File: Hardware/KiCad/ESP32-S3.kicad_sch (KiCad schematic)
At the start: 34 parts, among them J1 UJ20-C-H-G-SMT-1-P16-TR, J4 RJ45, U1 ESP32-S3-WROOM-1, U5 WE-TVS-82400102, U7 AP7333-33SRG-7

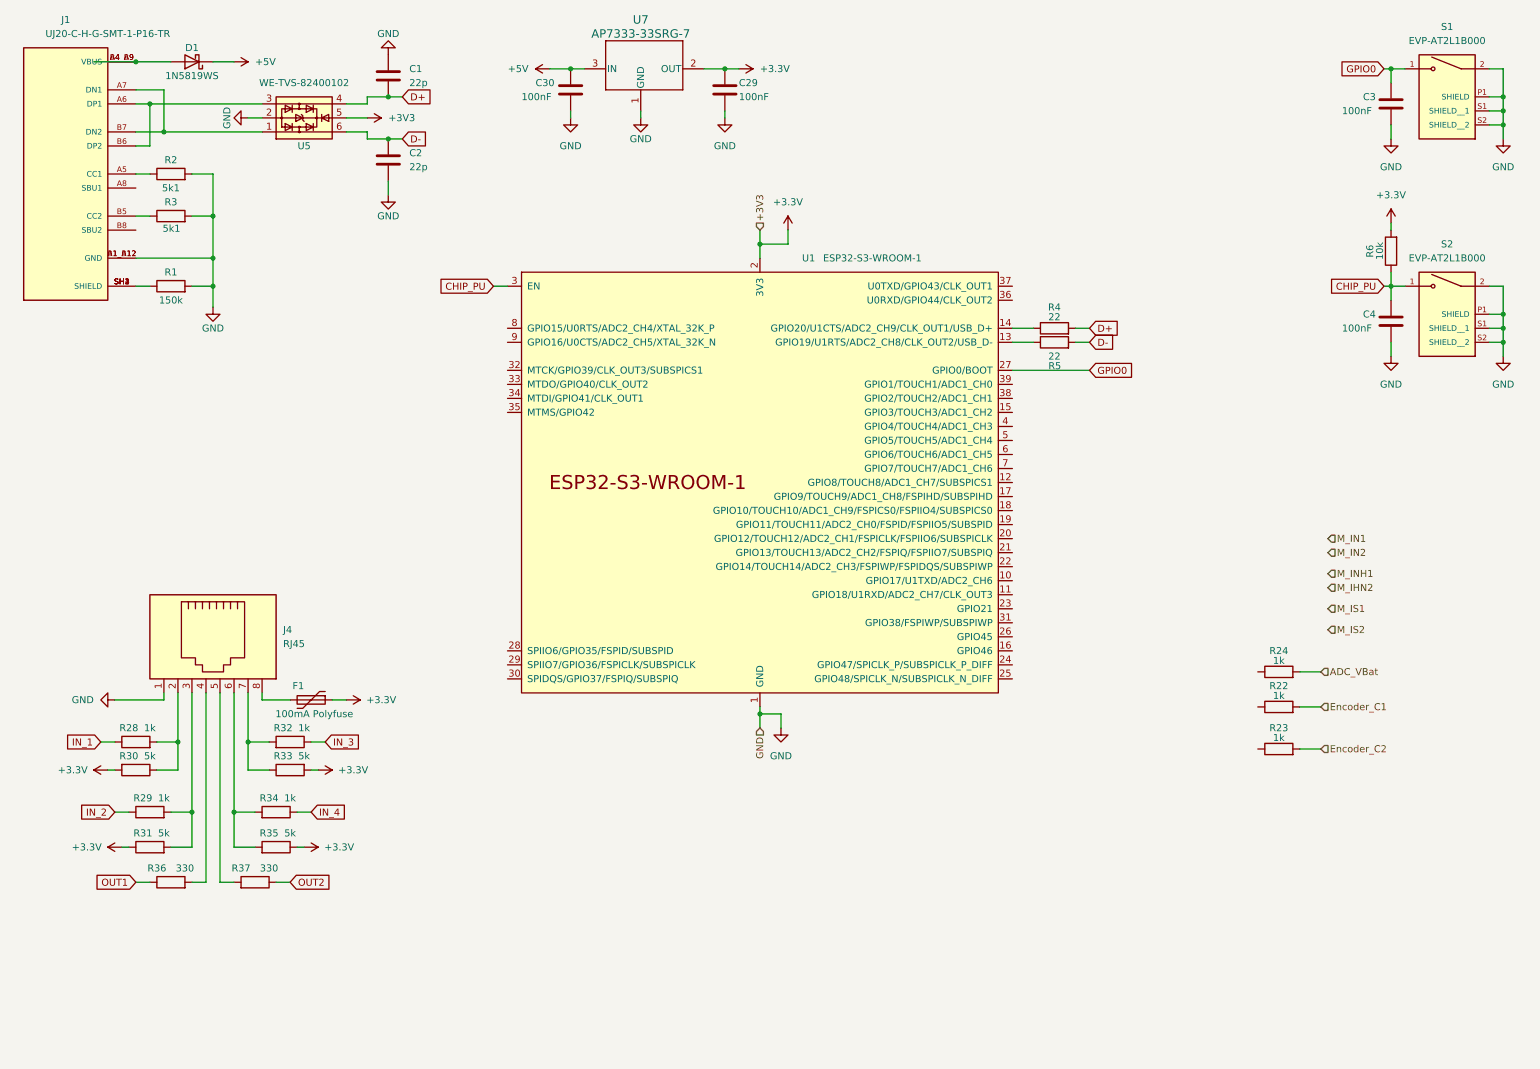
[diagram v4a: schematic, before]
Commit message: add ESD protection to inputs
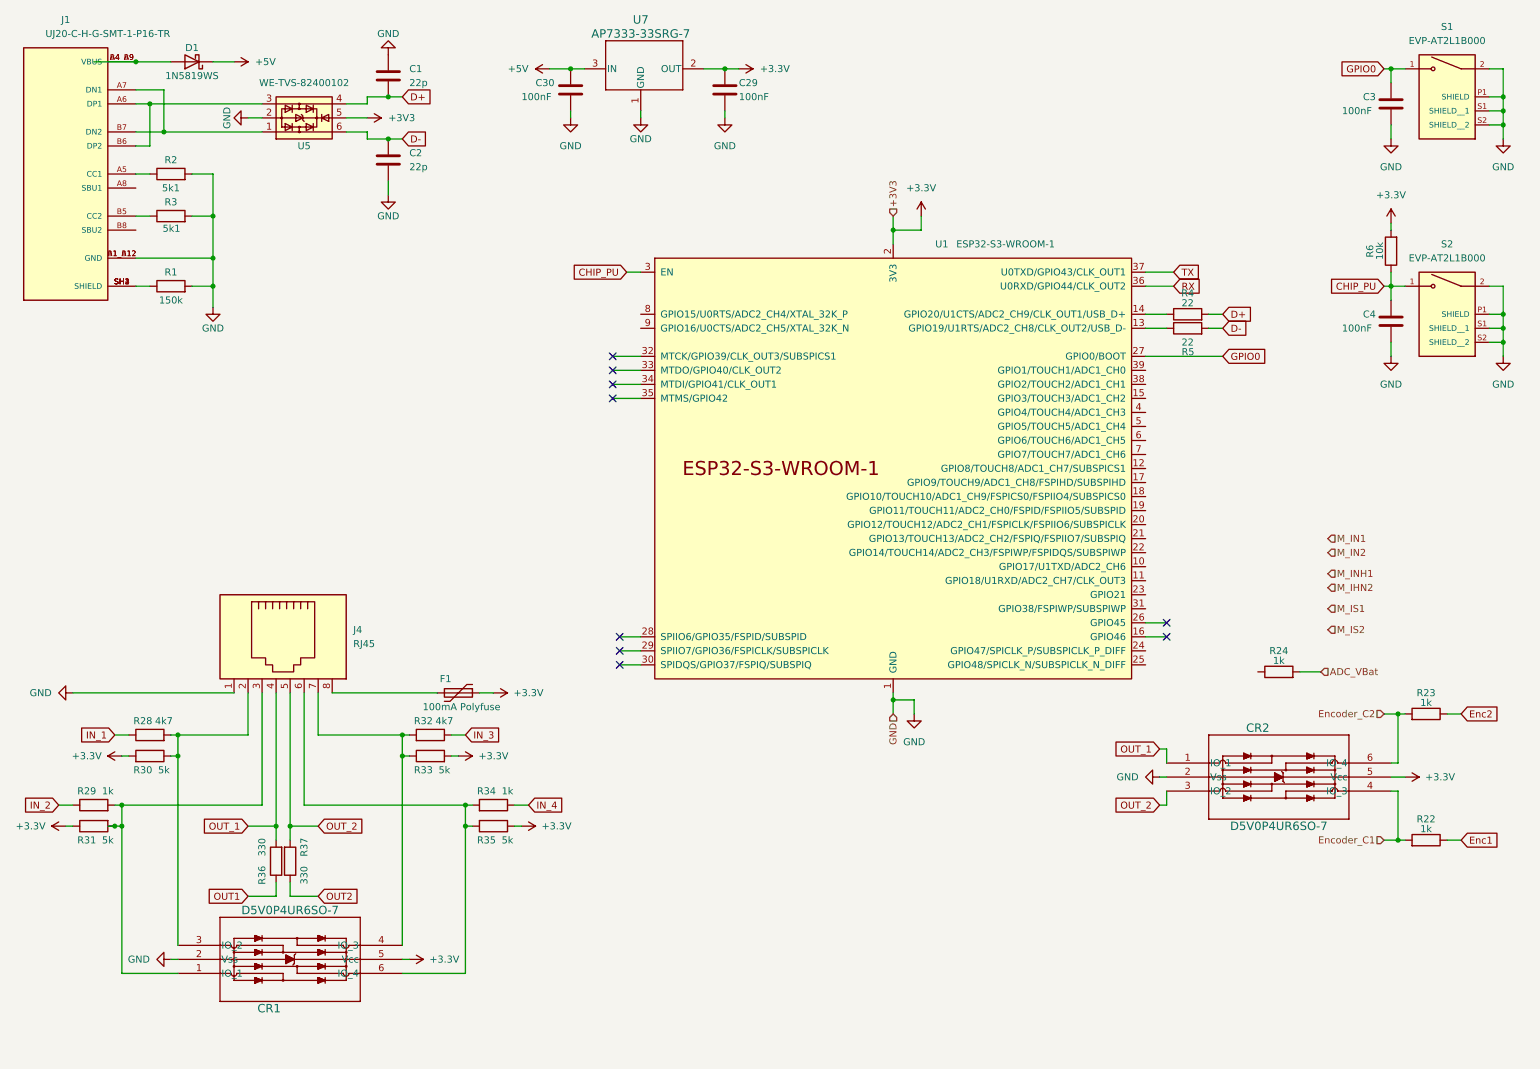
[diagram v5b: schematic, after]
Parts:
- added CR1, CR2: D5V0P4UR6SO-7, BugWiper_lib:SOT26_DIO, symbol BugWiper_Lib:D5V0P4UR6SO-7
- R28, R32: value 1k -> 4k7
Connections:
- net +3.3V: now also CR1.5 (Vcc), CR2.5 (Vcc)
- net Encoder_C1: now also CR2.4 (IO_3)
- net Encoder_C2: now also CR2.6 (IO_4)
- net GND: now also CR1.2 (Vss), CR2.2 (Vss)
- net at J4.7, R32.2, R33.1: now also CR1.4 (IO_3)
- net at J4.2, R28.2, R30.1: now also CR1.3 (IO_2)
- net at J4.3, R29.2, R31.2: now also CR1.1 (IO_1)
- net OUT_1: now reaches J4.4, R36.2
- net OUT_1: now also CR2.1 (IO_1)
- net OUT_2: now reaches J4.5, R37.2
- net OUT_2: now also CR2.3 (IO_2)
- net at J4.6, R34.2, R35.2: now also CR1.6 (IO_4)
- net RX: now reaches U1.36 (U0RXD/GPIO44/CLK_OUT2)
- net TX: now reaches U1.37 (U0TXD/GPIO43/CLK_OUT1)
- net Enc1: now reaches R22.1
- net Enc2: now reaches R23.1
- no-connect marks 0 -> 9
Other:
- moved on the sheet: F1, J4, R22, R23, R28, R29, R30, R31, R32, R33, R34, R35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

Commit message: add debug connector, arrange foodprints and add NTC and connect to GPIOs to ESP32
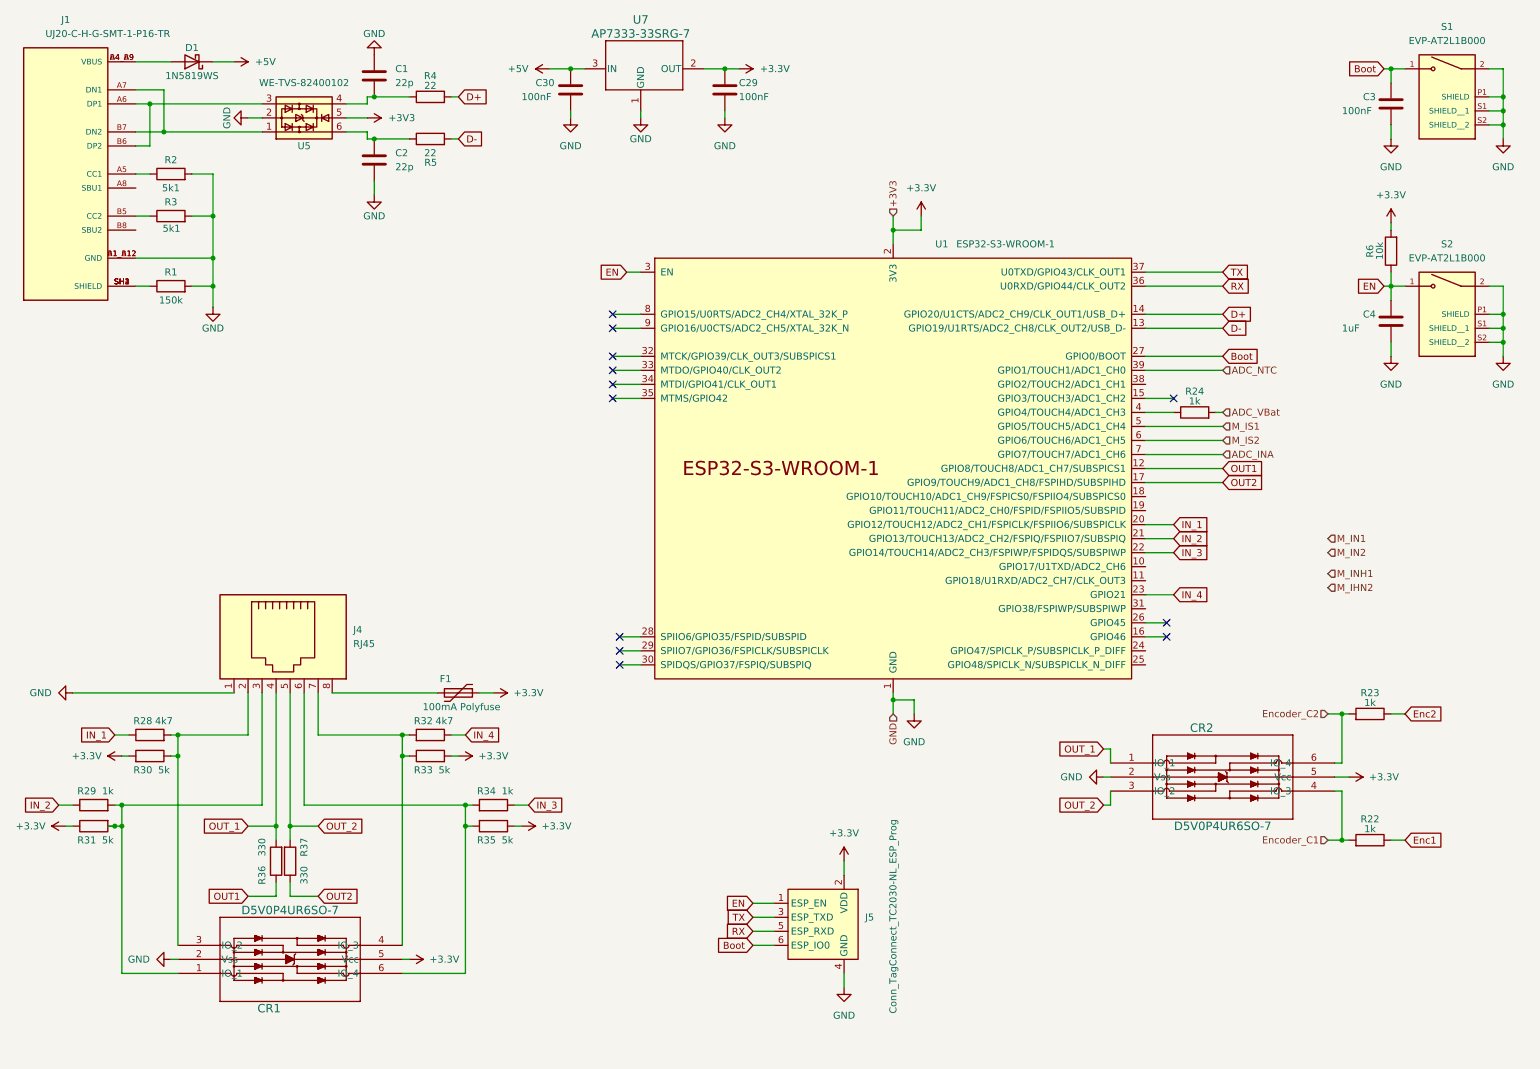
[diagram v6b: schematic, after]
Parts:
- added J5: Conn_TagConnect_TC2030-NL_ESP_Prog, Connector:Tag-Connect_TC2030-IDC-NL_2x03_P1.27mm_Vertical, symbol BugWiper_Lib:Conn_TagConnect_TC2030-NL_ESP_Prog
- C4: value 100nF -> 1uF
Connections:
- net +3.3V: now also J5.2 (VDD)
- net D+: now also U1.14 (GPIO20/U1CTS/ADC2_CH9/CLK_OUT1/USB_D+); no longer C1.2, U5.4
- net D-: now also U1.13 (GPIO19/U1RTS/ADC2_CH8/CLK_OUT2/USB_D-); no longer C2.1, U5.6
- net GND: now also J5.4 (GND)
- net IN_1: now also U1.20 (GPIO12/TOUCH12/ADC2_CH1/FSPICLK/FSPIIO6/SUBSPICLK)
- net IN_2: now also U1.21 (GPIO13/TOUCH13/ADC2_CH2/FSPIQ/FSPIIO7/SUBSPIQ)
- net IN_3: now also R34.1, U1.22 (GPIO14/TOUCH14/ADC2_CH3/FSPIWP/FSPIDQS/SUBSPIWP); no longer R32.1
- net IN_4: now also R32.1, U1.23 (GPIO21); no longer R34.1
- net M_IS1: now also U1.5 (GPIO5/TOUCH5/ADC1_CH4)
- net M_IS2: now also U1.6 (GPIO6/TOUCH6/ADC1_CH5)
- net OUT1: now also U1.12 (GPIO8/TOUCH8/ADC1_CH7/SUBSPICS1)
- net OUT2: now also U1.17 (GPIO9/TOUCH9/ADC1_CH8/FSPIHD/SUBSPIHD)
- net RX: now also J5.5 (ESP_RXD)
- net TX: now also J5.3 (ESP_TXD)
- net at R4.1: now also C1.2, U5.4; no longer U1.14 (GPIO20/U1CTS/ADC2_CH9/CLK_OUT1/USB_D+)
- net at R5.1: now also C2.1, U5.6; no longer U1.13 (GPIO19/U1RTS/ADC2_CH8/CLK_OUT2/USB_D-)
- net ADC_NTC: now reaches U1.39 (GPIO1/TOUCH1/ADC1_CH0)
- net at U1.4 (GPIO4/TOUCH4/ADC1_CH3): now also R24.1
- net ADC_INA: now reaches U1.7 (GPIO7/TOUCH7/ADC1_CH6)
- net CHIP_PU renamed EN
- net EN: now also J5.1 (ESP_EN)
- net GPIO0 renamed Boot
- net Boot: now also J5.6 (ESP_IO0)
- no-connect marks 9 -> 12
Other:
- moved on the sheet: C1, C2, CR2, R22, R23, R24

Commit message: add resistor arrays
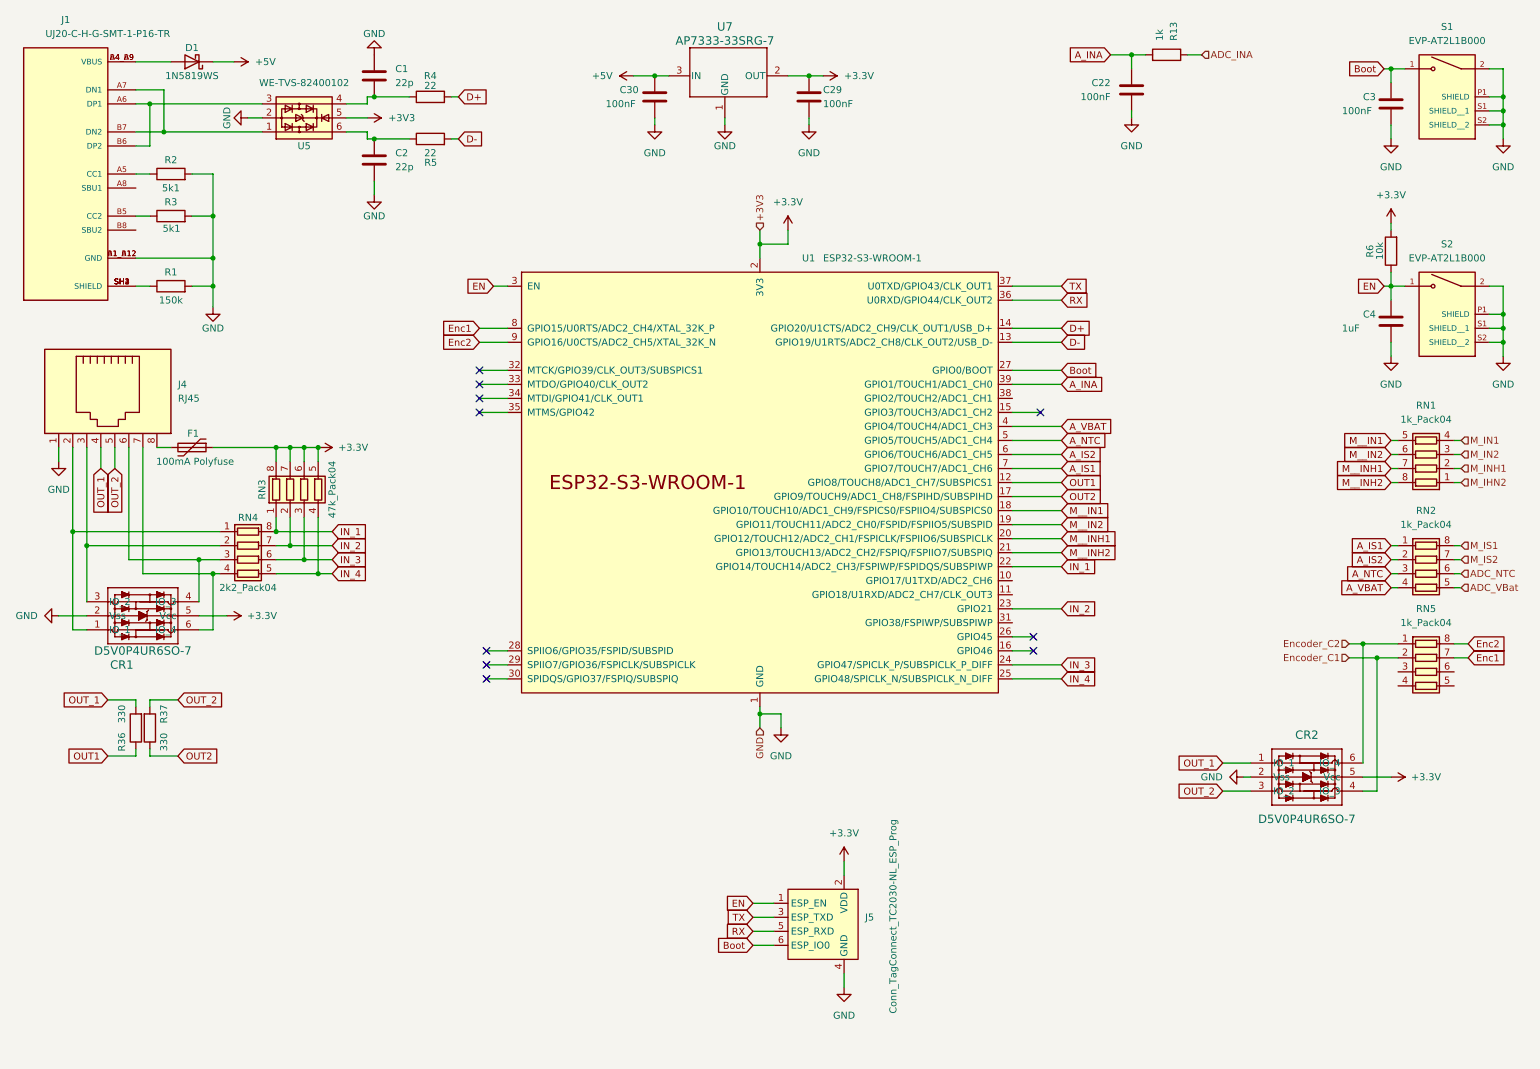
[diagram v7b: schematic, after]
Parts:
- removed R22, R23, R24, R29, R34: 1k, Resistor_SMD:R_0603_1608Metric, symbol Device:R
- removed R28, R32: 4k7, Resistor_SMD:R_0603_1608Metric, symbol Device:R
- removed R30, R31, R33, R35: 5k, Resistor_SMD:R_0603_1608Metric, symbol Device:R
- added C22: 100nF, Capacitor_SMD:C_0603_1608Metric, symbol Device:C
- added R13: 1k, Resistor_SMD:R_0603_1608Metric, symbol Device:R
- added RN1, RN2, RN5: 1k_Pack04, BugWiper_lib:BO_CAY16, symbol Device:R_Pack04
- added RN3: 47k_Pack04, BugWiper_lib:BO_CAY16, symbol Device:R_Pack04
- added RN4: 2k2_Pack04, BugWiper_lib:BO_CAY16, symbol Device:R_Pack04
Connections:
- net +3.3V: now also RN3.5 (R4.2), RN3.6 (R3.2), RN3.7 (R2.2), RN3.8 (R1.2)
- net ADC_INA: now also R13.1; no longer U1.7 (GPIO7/TOUCH7/ADC1_CH6)
- net ADC_NTC: now also RN2.6 (R3.2); no longer U1.39 (GPIO1/TOUCH1/ADC1_CH0)
- net ADC_VBat: now also RN2.5 (R4.2)
- net Enc1: now also U1.8 (GPIO15/U0RTS/ADC2_CH4/XTAL_32K_P), RN5.7 (R2.2)
- net Enc2: now also U1.9 (GPIO16/U0CTS/ADC2_CH5/XTAL_32K_N), RN5.8 (R1.2)
- net Encoder_C1: now also RN5.2 (R2.1)
- net Encoder_C2: now also RN5.1 (R1.1)
- net GND: now also C22.2
- net IN_1: now also U1.22 (GPIO14/TOUCH14/ADC2_CH3/FSPIWP/FSPIDQS/SUBSPIWP), RN3.1 (R1.1), RN4.8 (R1.2); no longer U1.20 (GPIO12/TOUCH12/ADC2_CH1/FSPICLK/FSPIIO6/SUBSPICLK)
- net IN_2: now also U1.23 (GPIO21), RN3.2 (R2.1), RN4.7 (R2.2); no longer U1.21 (GPIO13/TOUCH13/ADC2_CH2/FSPIQ/FSPIIO7/SUBSPIQ)
- net IN_3: now also U1.24 (GPIO47/SPICLK_P/SUBSPICLK_P_DIFF), RN3.3 (R3.1), RN4.6 (R3.2); no longer U1.22 (GPIO14/TOUCH14/ADC2_CH3/FSPIWP/FSPIDQS/SUBSPIWP)
- net IN_4: now also U1.25 (GPIO48/SPICLK_N/SUBSPICLK_N_DIFF), RN3.4 (R4.1), RN4.5 (R4.2); no longer U1.23 (GPIO21)
- net M_IHN2: now also RN1.1 (R1.1)
- net M_IN1: now also RN1.4 (R4.1)
- net M_IN2: now also RN1.3 (R3.1)
- net M_INH1: now also RN1.2 (R2.1)
- net M_IS1: now also RN2.8 (R1.2); no longer U1.5 (GPIO5/TOUCH5/ADC1_CH4)
- net M_IS2: now also RN2.7 (R2.2); no longer U1.6 (GPIO6/TOUCH6/ADC1_CH5)
- net at CR1.4 (IO_3): now also J4.6, RN4.3 (R3.1); no longer J4.7
- net at J4.2: now also CR1.1 (IO_1), RN4.1 (R1.1); no longer CR1.3 (IO_2)
- net at J4.3: now also CR1.3 (IO_2), RN4.2 (R2.1); no longer CR1.1 (IO_1)
- net at CR1.6 (IO_4): now also J4.7, RN4.4 (R4.1); no longer J4.6
- net M__IN1: now reaches U1.18 (GPIO10/TOUCH10/ADC1_CH9/FSPICS0/FSPIIO4/SUBSPICS0)
- net M__IN1: now also RN1.5 (R4.2)
- net M__IN2: now reaches U1.19 (GPIO11/TOUCH11/ADC2_CH0/FSPID/FSPIIO5/SUBSPID)
- net M__IN2: now also RN1.6 (R3.2)
- net A_VBAT: now reaches U1.4 (GPIO4/TOUCH4/ADC1_CH3)
- net A_VBAT: now also RN2.4 (R4.1)
- new net A_INA: C22.1, R13.2, U1.39 (GPIO1/TOUCH1/ADC1_CH0)
- new net A_IS1: RN2.1 (R1.1), U1.7 (GPIO7/TOUCH7/ADC1_CH6)
- new net A_IS2: RN2.2 (R2.1), U1.6 (GPIO6/TOUCH6/ADC1_CH5)
- new net A_NTC: RN2.3 (R3.1), U1.5 (GPIO5/TOUCH5/ADC1_CH4)
- new net M__INH1: RN1.7 (R2.2), U1.20 (GPIO12/TOUCH12/ADC2_CH1/FSPICLK/FSPIIO6/SUBSPICLK)
- new net M__INH2: RN1.8 (R1.2), U1.21 (GPIO13/TOUCH13/ADC2_CH2/FSPIQ/FSPIIO7/SUBSPIQ)
- no-connect marks 12 -> 10
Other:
- moved on the sheet: C29, C30, CR1, CR2, F1, J4, R36, R37, U1, U7

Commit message: begin routing
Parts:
- removed R36, R37: 330, Resistor_SMD:R_0603_1608Metric, symbol Device:R
- added RN6: 100R_Pack04, BugWiper_lib:BO_CAY16, symbol Device:R_Pack04
- added RN7: 100R_Pack04, Resistor_THT:R_Array_SIP8, symbol Device:R_Pack04_Split
- D1: footprint Diode_SMD:D_SOD-323 -> Diode_SMD:D_SOD-323_HandSoldering
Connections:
- net Enc1: now also RN5.8 (R1.2); no longer RN5.7 (R2.2)
- net Enc2: now also RN5.7 (R2.2); no longer RN5.8 (R1.2)
- net Encoder_C1: now also RN7.1 (R1.1); no longer CR2.4 (IO_3), RN5.2 (R2.1)
- net Encoder_C2: now also RN7.2 (R2.1); no longer CR2.6 (IO_4), RN5.1 (R1.1)
- net OUT_1: now also RN7.6 (R3.2); no longer J4.4
- net OUT_2: now also RN7.5 (R4.2); no longer J4.5
- new net: CR1.6 (IO_4), RN4.1 (R1.1), RN6.8 (R1.2)
- new net: CR1.4 (IO_3), RN4.2 (R2.1), RN6.7 (R2.2)
- new net: CR1.1 (IO_1), RN4.3 (R3.1), RN6.6 (R3.2)
- new net: CR1.3 (IO_2), RN4.4 (R4.1), RN6.5 (R4.2)
- new net: J4.2, RN7.3 (R3.1)
- new net: J4.4, RN6.1 (R1.1)
- new net: J4.5, RN6.2 (R2.1)
- new net: J4.6, RN6.3 (R3.1)
- new net: J4.7, RN6.4 (R4.1)
- new net: CR2.4 (IO_3), RN5.2 (R2.1), RN7.7 (R2.2)
- new net: J4.3, RN7.4 (R4.1)
- new net: CR2.6 (IO_4), RN5.1 (R1.1), RN7.8 (R1.2)
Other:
- moved on the sheet: CR1, CR2, F1, RN3, RN4, RN5
